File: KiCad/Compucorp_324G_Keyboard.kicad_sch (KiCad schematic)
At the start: 49 parts, among them J3 To Scan Board, SW1 e^x 10^x, SW10 2nd FUNC, SW11 ARCTAN, SW12 a^x, SW13 5, SW14 EXCHn, SW15 START/STOP, SW16 x,y → Θ,r, SW17 DIV, SW18 EXP, SW19 4, SW2 ), SW20 RCLn, SW21 CLEAR ENTRY, SW22 º → R → º, SW23 ARCSIN ARCCOS, SW24 MUL, SW25 CHG SIGN, SW26 3, SW27 STn, SW28 RESET, SW29 TAN, SW3 DEC → D.MS, SW30 INV, SW31 MINUS, SW32 DP, SW33 2, SW34 Θ,r → x,y, SW35 SQRT, SW36 PLUS, SW37 9, SW38 1, SW39 SIN COS, SW4 7, SW40 PI, SW41 EQUALS, SW42 8, SW43 0, SW44 FED/MUNI, SW45 RUN/LOAD, SW46 PROG 1/2, SW47 RUN/STEP/LOAD, SW48 GRAD/DEG, SW5 Ln LOG, SW6 (, SW7 D.MS → DEC, SW8 6, SW9 SET DP

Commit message: Started Memory Board schematic
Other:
- title: Compucorp 320-Series Keyboard -> Compucorp 300-Series Keyboard
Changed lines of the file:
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@@
 	(generator "eeschema")
 	(generator_version "9.0")
-	(paper "A4")
+	(paper "A3")
 	(title_block
-		(title "Compucorp 320-Series Keyboard")
+		(title "Compucorp 300-Series Keyboard")
 		(date "1/FEB/2026")
 		(rev "WIP")

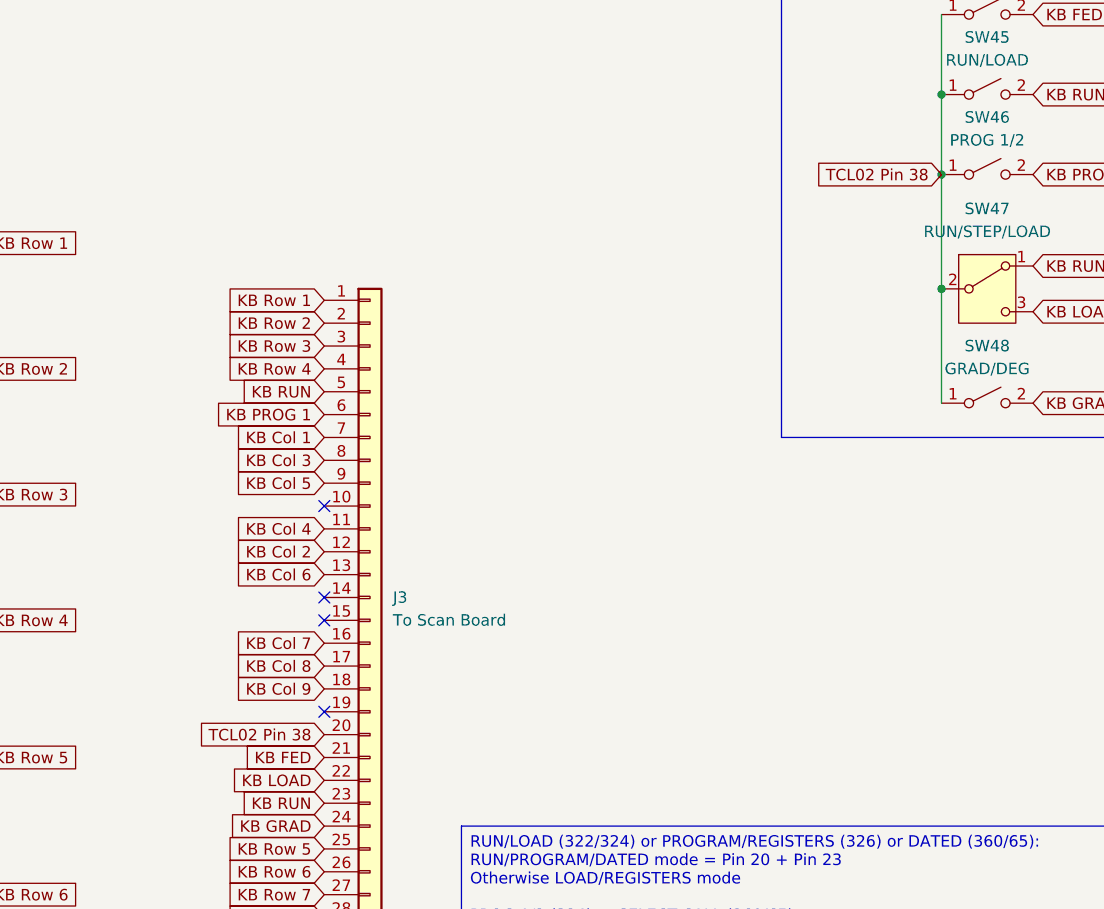
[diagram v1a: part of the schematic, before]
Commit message: Schematic updates
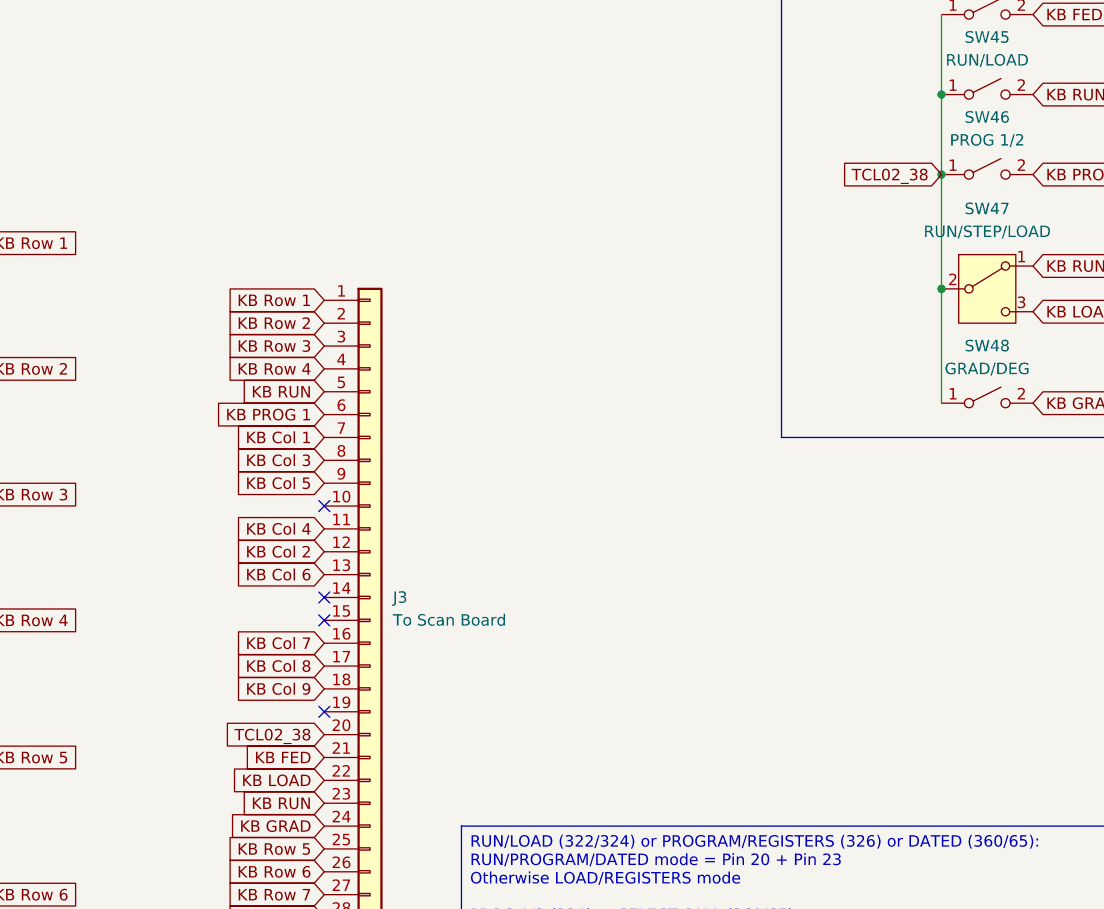
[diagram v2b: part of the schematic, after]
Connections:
- net TCL02 Pin 38 renamed TCL02_38
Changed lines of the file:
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@@
 		)
 	)
-	(global_label "TCL02 Pin 38"
+	(global_label "TCL02_38"
 		(shape input)
 		(at 187.96 107.95 180)
@@
 		)
 		(property "Intersheetrefs" "${INTERSHEET_REFS}"
-			(at 171.9121 107.95 0)
+			(at 175.9035 107.95 0)
 			(effects
 				(font
@@
 		)
 	)
-	(global_label "TCL02 Pin 38"
+	(global_label "TCL02_38"
 		(shape input)
 		(at 256.54 45.72 180)
@@
 		)
 		(property "Intersheetrefs" "${INTERSHEET_REFS}"
-			(at 240.4921 45.72 0)
-			(effects
-				(font
+			(at 244.4835 45.72 0)
+			(effects
+				(font
